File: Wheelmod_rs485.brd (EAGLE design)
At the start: 42 x 40 mm, 52 parts, among them IC1 SN75176BPSR, SW1 RST_SW, SW2 HWB_SW, U1 ATMEGA8U2AU, U2 SI8441IS1, U3 MC33887-HSOP, U4 NFET-SOIC8, U5 LDO, X1 MINI-USB, X3 ENC, X5 LOGIC_IN, Y1 SMDRESONATOR

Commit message: Some changes to board and gerber files for production.
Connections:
- removed net N$22: F1.1, X2.1
- new net N$32: F1.1, X2.2
- net B: now also X2.4; no longer X2.2
- net GND: now also X2.1; no longer X2.4
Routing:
- net N$22: track 5.64 -> 0.00 mm
- net N$32: track 0.00 -> 2.57 mm
- net B: track 10.7 -> 9.21 mm
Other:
- board text added: "v0.7"
- board text removed: "v0.6"
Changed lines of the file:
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@@
 <?xml version="1.0" encoding="utf-8"?>
 <!DOCTYPE eagle SYSTEM "eagle.dtd">
-<eagle version="6.5.0">
+<eagle version="7.0.0">
 <drawing>
 <settings>
@@
 <grid distance="0.1" unitdist="mm" unit="mm" style="lines" multiple="1" display="yes" altdistance="0.05" altunitdist="mm" altunit="mm"/>
 <layers>
-<layer number="1" name="Top" color="4" fill="1" visible="no" active="yes"/>
+<layer number="1" name="Top" color="4" fill="1" visible="yes" active="yes"/>
 <layer number="16" name="Bottom" color="1" fill="1" visible="yes" active="yes"/>
 <layer number="17" name="Pads" color="2" fill="1" visible="yes" active="yes"/>
 <layer number="18" name="Vias" color="2" fill="1" visible="yes" active="yes"/>
-<layer number="19" name="Unrouted" color="6" fill="1" visible="no" active="yes"/>
-<layer number="20" name="Dimension" color="15" fill="1" visible="no" active="yes"/>
-<layer number="21" name="tPlace" color="7" fill="1" visible="no" active="yes"/>
+<layer number="19" name="Unrouted" color="6" fill="1" visible="yes" active="yes"/>
+<layer number="20" name="Dimension" color="15" fill="1" visible="yes" active="yes"/>
+<layer number="21" name="tPlace" color="7" fill="1" visible="yes" active="yes"/>
 <layer number="22" name="bPlace" color="7" fill="1" visible="yes" active="yes"/>
-<layer number="23" name="tOrigins" color="15" fill="1" visible="no" active="yes"/>
+<layer number="23" name="tOrigins" color="15" fill="1" visible="yes" active="yes"/>
 <layer number="24" name="bOrigins" color="15" fill="1" visible="yes" active="yes"/>
 <layer number="25" name="tNames" color="7" fill="1" visible="no" active="yes"/>
-<layer number="26" name="bNames" color="7" fill="1" visible="yes" active="yes"/>
+<layer number="26" name="bNames" color="7" fill="1" visible="no" active="yes"/>
 <layer number="27" name="tValues" color="7" fill="1" visible="no" active="yes"/>
 <layer number="28" name="bValues" color="7" fill="1" visible="no" active="yes"/>
@@
 <layer number="46" name="Milling" color="3" fill="1" visible="no" active="yes"/>
 <layer number="47" name="Measures" color="7" fill="1" visible="no" active="yes"/>
-<layer number="48" name="Document" color="7" fill="1" visible="no" active="yes"/>
+<layer number="48" name="Document" color="7" fill="1" visible="yes" active="yes"/>
 <layer number="49" name="Reference" color="7" fill="1" visible="no" active="yes"/>
 <layer number="50" name="dxf" color="7" fill="1" visible="no" active="no"/>
-<layer number="51" name="tDocu" color="7" fill="1" visible="no" active="yes"/>
+<layer number="51" name="tDocu" color="7" fill="1" visible="yes" active="yes"/>
 <layer number="52" name="bDocu" color="7" fill="1" visible="yes" active="yes"/>
 <layer number="53" name="tGND_GNDA" color="7" fill="9" visible="no" active="no"/>
@@
 <text x="21.7" y="34.1" size="1.6" layer="48">MOTOR</text>
 <text x="1.8" y="15.6" size="1.6" layer="48">DCH</text>
-<text x="34.5" y="31.3" size="2" layer="48" rot="SR0">v0.6</text>
+<text x="34.5" y="31.3" size="2" layer="48" rot="SR0">v0.7</text>
 <polygon width="0.2" layer="42">
 <vertex x="10.9" y="14.9"/>
@@
 <hole x="4.8" y="33.53" drill="1.2"/>
 <hole x="19.01" y="31.05" drill="1.2"/>
-<text x="7.27" y="36.91" size="1.778" layer="48" rot="R270">RS485</text>
-<text x="12.53" y="35.22" size="1.778" layer="48">GPIO</text>
+<text x="4.59" y="34.37" size="1.6" layer="48">RS485</text>
+<text x="13.53" y="34.42" size="1.6" layer="48">GPIO</text>
 </plain>
 <attributes>
@@
 <pass name="Default">
 <param name="RoutingGrid" value="50mil"/>
+<param name="AutoGrid" value="1"/>
+<param name="Efforts" value="0"/>
+<param name="TopRouterVariant" value="1"/>
 <param name="tpViaShape" value="round"/>
 <param name="PrefDir.1" value="|"/>
@@
 <via x="1.2" y="33" extent="1-16" drill="0.5"/>
 <contactref element="IC1" pad="5"/>
-<contactref element="X2" pad="4"/>
 <contactref element="C15" pad="2"/>
 <via x="5.8" y="16.4" extent="1-16" drill="0.5"/>
 <via x="4.7" y="15.3" extent="1-16" drill="0.5"/>
 <via x="14.43" y="24.72" extent="1-16" drill="0.5"/>
+<contactref element="X2" pad="1"/>
 </signal>
 <signal name="N$6">
@@
 <wire x1="17.1234" y1="17.765" x2="20.965" y2="17.765" width="0.5" layer="1"/>
 <wire x1="20.965" y1="17.765" x2="21.9" y2="18.7" width="0.5" layer="1"/>
-<wire x1="21.9" y1="18.7" x2="21.8" y2="25.3" width="0.5" layer="1"/>
-<wire x1="21.8" y1="25.3" x2="24.4" y2="27.9" width="0.5" layer="1"/>
+<wire x1="21.9" y1="18.7" x2="21.9" y2="25.4" width="0.5" layer="1"/>
+<wire x1="21.9" y1="25.4" x2="24.4" y2="27.9" width="0.5" layer="1"/>
 <wire x1="24.4" y1="27.9" x2="34.9" y2="27.9" width="0.5" layer="1"/>
 <wire x1="34.9" y1="27.9" x2="36.2" y2="26.6" width="0.5" layer="1"/>
@@
 <wire x1="12.49" y1="21.99" x2="12.49" y2="19.9826" width="0.5" layer="16"/>
 </signal>
-<signal name="N$22">
-<contactref element="X2" pad="1"/>
-<contactref element="F1" pad="1"/>
-<wire x1="2.98" y1="31.725" x2="6.265" y2="31.725" width="0.6" layer="1"/>
-<wire x1="6.265" y1="31.725" x2="7.93" y2="30.06" width="0.6" layer="1"/>
-</signal>
 <signal name="B">
 <contactref element="IC1" pad="7"/>
-<contactref element="X2" pad="2"/>
 <contactref element="R5" pad="2"/>
 <wire x1="9.54" y1="32.38" x2="9.2" y2="32.56" width="0.5" layer="16"/>
 <wire x1="10.35" y1="30.0458" x2="10.335" y2="30.0308" width="0.5" layer="16"/>
-<wire x1="5.52" y1="30.455" x2="5.52" y2="32.21" width="0.5" layer="16"/>
-<wire x1="5.52" y1="32.21" x2="7.16" y2="33.85" width="0.5" layer="16"/>
-<wire x1="7.16" y1="33.85" x2="8.95" y2="33.85" width="0.5" layer="16"/>
-<wire x1="8.95" y1="33.85" x2="9.56" y2="33.24" width="0.5" layer="16"/>
-<wire x1="9.56" y1="33.24" x2="9.56" y2="32.4" width="0.5" layer="16"/>
 <wire x1="9.56" y1="32.4" x2="9.54" y2="32.38" width="0.5" layer="16"/>
 <wire x1="9.54" y1="32.38" x2="9.54" y2="32.11" width="0.5" layer="16"/>
@@
 <wire x1="10.31" y1="31.34" x2="10.31" y2="30.0558" width="0.5" layer="16"/>
 <wire x1="10.31" y1="30.0558" x2="10.335" y2="30.0308" width="0.5" layer="16"/>
+<contactref element="X2" pad="4"/>
+<wire x1="5.52" y1="27.915" x2="8.915" y2="27.915" width="0.4" layer="16"/>
+<wire x1="8.915" y1="27.915" x2="10.3" y2="29.3" width="0.4" layer="16"/>
+<wire x1="10.3" y1="29.3" x2="10.3" y2="29.9958" width="0.4" layer="16"/>
+<wire x1="10.3" y1="29.9958" x2="10.335" y2="30.0308" width="0.4" layer="16"/>
 </signal>
 <signal name="A">
 <contactref element="IC1" pad="6"/>
-<contactref element="X2" pad="3"/>
 <contactref element="R5" pad="1"/>
-<wire x1="2.98" y1="29.185" x2="6.045" y2="29.185" width="0.5" layer="16"/>
-<wire x1="6.045" y1="29.185" x2="6.95" y2="30.09" width="0.5" layer="16"/>
-<wire x1="6.95" y1="30.09" x2="6.95" y2="31.49" width="0.5" layer="16"/>
-<wire x1="6.95" y1="31.49" x2="7.84" y2="32.38" width="0.5" layer="16"/>
 <wire x1="9.065" y1="30.0308" x2="9.065" y2="31.155" width="0.5" layer="16"/>
 <wire x1="9.065" y1="31.155" x2="7.84" y2="32.38" width="0.5" layer="16"/>
+<contactref element="X2" pad="3"/>
+<wire x1="2.98" y1="29.185" x2="5.815" y2="29.185" width="0.4" layer="16"/>
+<wire x1="5.815" y1="29.185" x2="6.4" y2="28.6" width="0.4" layer="16"/>
+<wire x1="6.4" y1="28.6" x2="8.4" y2="28.6" width="0.4" layer="16"/>
+<wire x1="8.4" y1="28.6" x2="9.1" y2="29.3" width="0.4" layer="16"/>
+<wire x1="9.1" y1="29.3" x2="9.1" y2="29.9958" width="0.4" layer="16"/>
+<wire x1="9.1" y1="29.9958" x2="9.065" y2="30.0308" width="0.4" layer="16"/>
 </signal>
 <signal name="N$24">
@@
 <wire x1="17.3" y1="32.775" x2="17.205" y2="32.87" width="0.5" layer="16"/>
 </signal>
+<signal name="N$32">
+<contactref element="X2" pad="2"/>
+<contactref element="F1" pad="1"/>
+<wire x1="7.93" y1="30.06" x2="5.915" y2="30.06" width="0.8" layer="1"/>
+<wire x1="5.915" y1="30.06" x2="5.52" y2="30.455" width="0.8" layer="1"/>
+</signal>
 </signals>

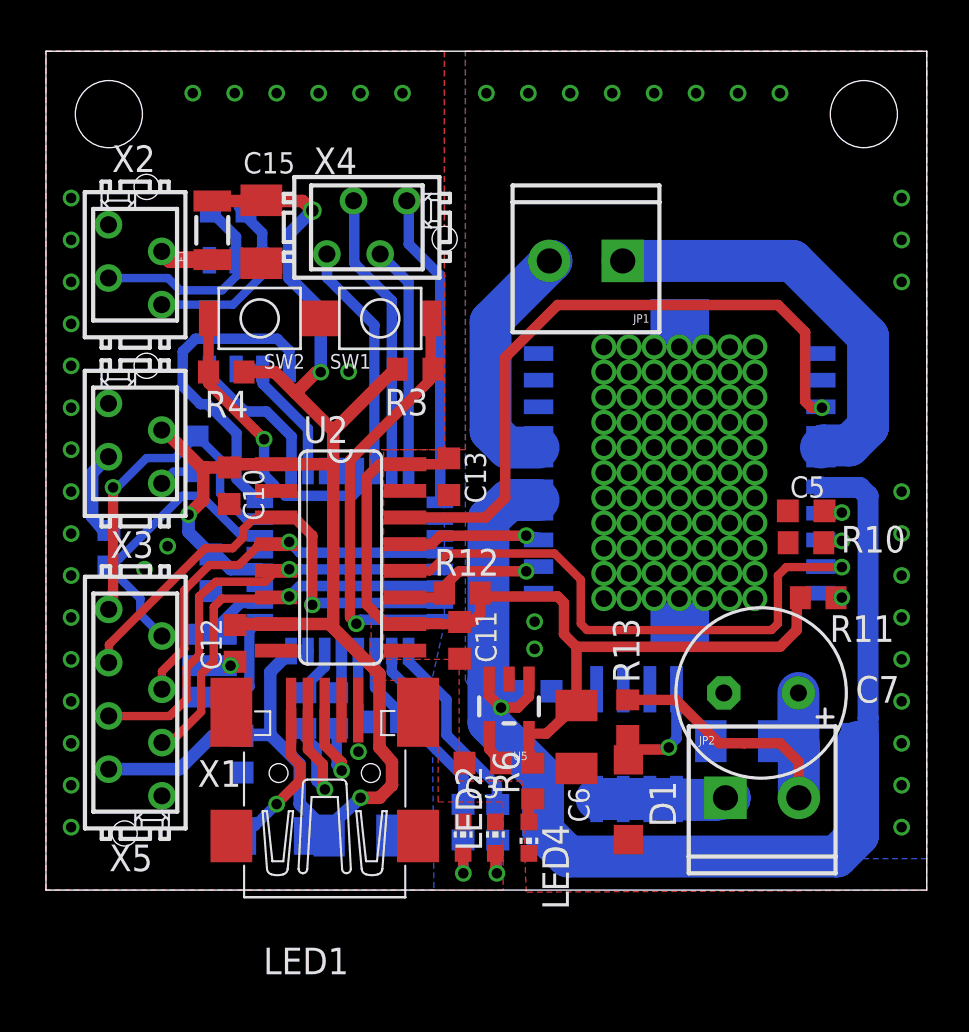
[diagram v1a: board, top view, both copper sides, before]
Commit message: Full duplex tugi kommunikatsioonimoodulit
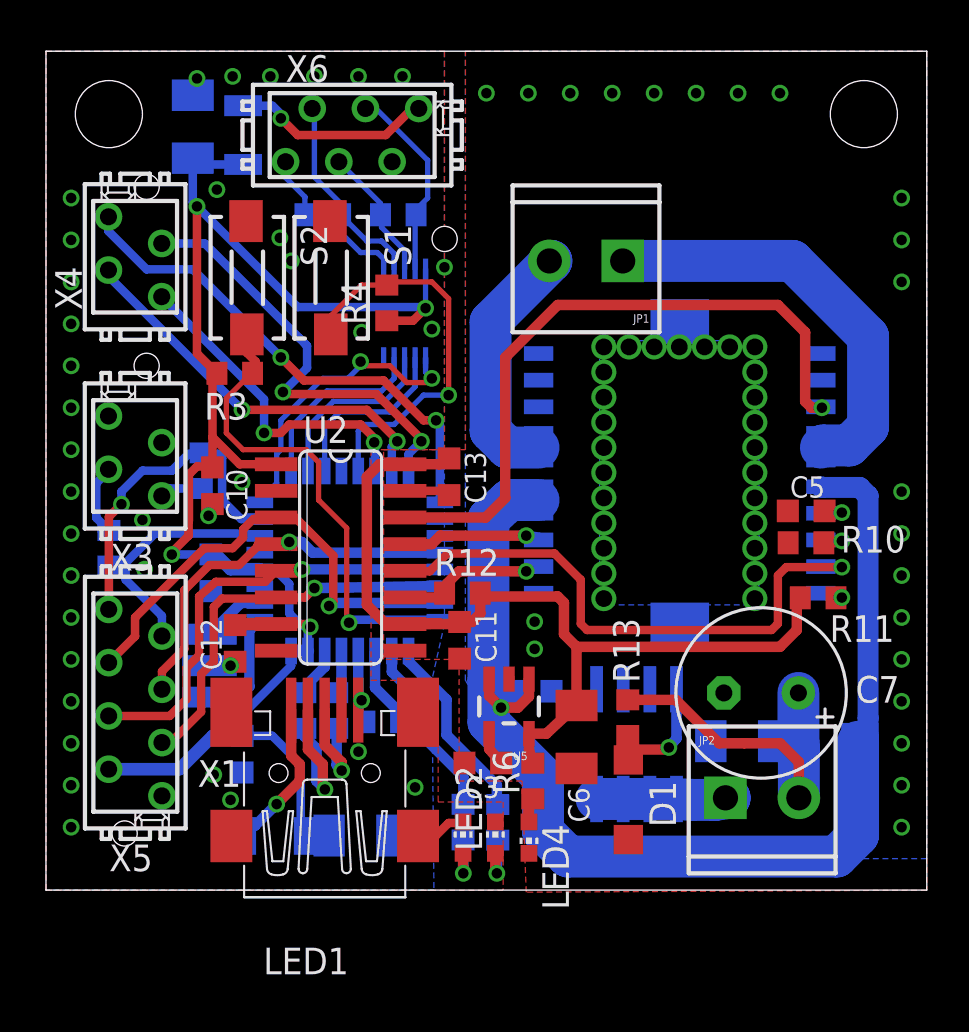
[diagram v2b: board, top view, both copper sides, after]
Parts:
- removed IC1: SN75176BPSR, rs485DRIVER:SO8
- removed SW1: RST_SW, Erik:SMD-TACT-3.9X2.9
- removed SW2: HWB_SW, Erik:SMD-TACT-3.9X2.9
- removed X2: (no value), con-amp-micromatch:MICROMATCH-4
- added R9: 120, rcl:R0603
- added S1: HWB, kommunikatsioonimoodul:ADTSM3
- added S2: RESET, kommunikatsioonimoodul:ADTSM3
- added U$1: SN65HVF76DGS, rs485:MSOP10
- added X6: R485-IO, con-amp-micromatch:MICROMATCH-6
- moved X4 11.1 mm to (4.25, 30.2), turned to 90 degrees
- moved R3 8.60 mm to (9.00, 24.6)
- moved R4 8.33 mm to (16.2, 28.0), turned to 270 degrees
- moved R5 8.11 mm to (16.8, 32.2)
- moved C15 5.98 mm to (7.00, 36.4), flipped to the bottom, turned to 90 degrees
- moved F1 4.77 mm to (9.40, 36.0), flipped to the bottom, turned to 270 degrees
- moved R17 0.82 mm to (7.40, 20.0)
- moved C10 0.80 mm to (7.94, 19.3)
- moved X3 0.60 mm to (4.25, 20.7)
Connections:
- removed net N$32: F1.1, X2.2
- new net N$33: F1.1, X6.1
- new net RE: U$1.2, U1.11
- new net Y: R9.1, U$1.6, X6.6
- new net Z: R9.2, U$1.7, X6.5
- net A: now also R5.2, U$1.9, X6.3; no longer IC1.6, R5.1, X2.3
- net B: now also R5.1, U$1.8, X6.4; no longer IC1.7, R5.2, X2.4
- net DE: now also U$1.3; no longer IC1.2, IC1.3
- net GND: now also S1.1, S2.1, U$1.5, X6.2; no longer IC1.5, SW1.1, SW2.2, X2.1, X3.1
- net N$10: now also S2.2; no longer SW1.2
- net N$2: now also S1.2; no longer SW2.1
- net RX: now also U$1.1; no longer IC1.1
- net TX: now also U$1.4; no longer IC1.4
- net VCC: now also U$1.10; no longer IC1.8, X3.2
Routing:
- net VCC: track 92.9 -> 81.9 mm
- net N$27: track 10.9 -> 20.9 mm, vias 0 -> 2
- net Z: track 0.00 -> 9.68 mm
- net N$33: track 0.00 -> 9.60 mm, vias 0 -> 1
- net N$31: track 15.0 -> 24.0 mm, vias 0 -> 2
- net RE: track 0.00 -> 8.60 mm
- net Y: track 0.00 -> 8.04 mm
- net N$26: track 13.6 -> 18.9 mm, vias 0 -> 2
- net N$2: track 14.5 -> 19.0 mm
- net N$24: track 11.3 -> 15.8 mm, vias 0 -> 2
- net B: track 9.21 -> 6.42 mm
- net N$10: track 20.4 -> 23.1 mm
- net N$32: track 2.57 -> 0.00 mm
- net GND: track 5.51 -> 7.94 mm, vias 27 -> 38
- net GNDA: track 0.03 -> 2.21 mm, vias 99 -> 49
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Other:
- board text added: "v0.8"
- board text removed: "v0.7"
